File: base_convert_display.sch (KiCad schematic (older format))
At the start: 42 parts

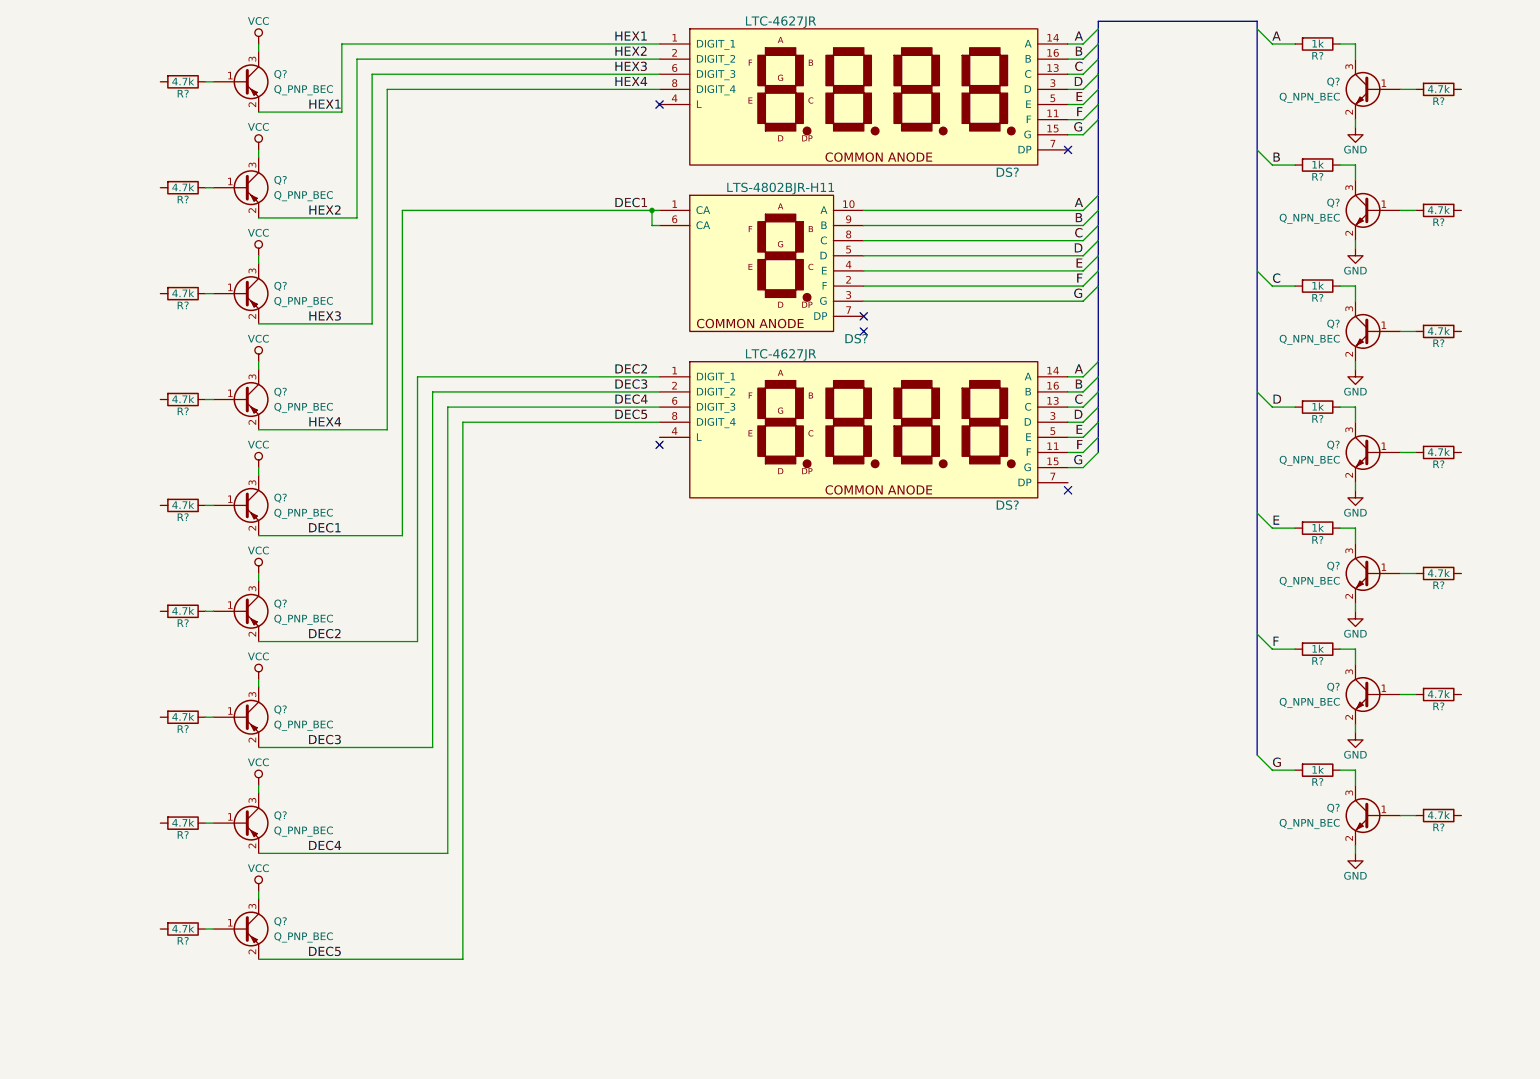
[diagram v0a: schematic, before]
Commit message: capture keypad inputs
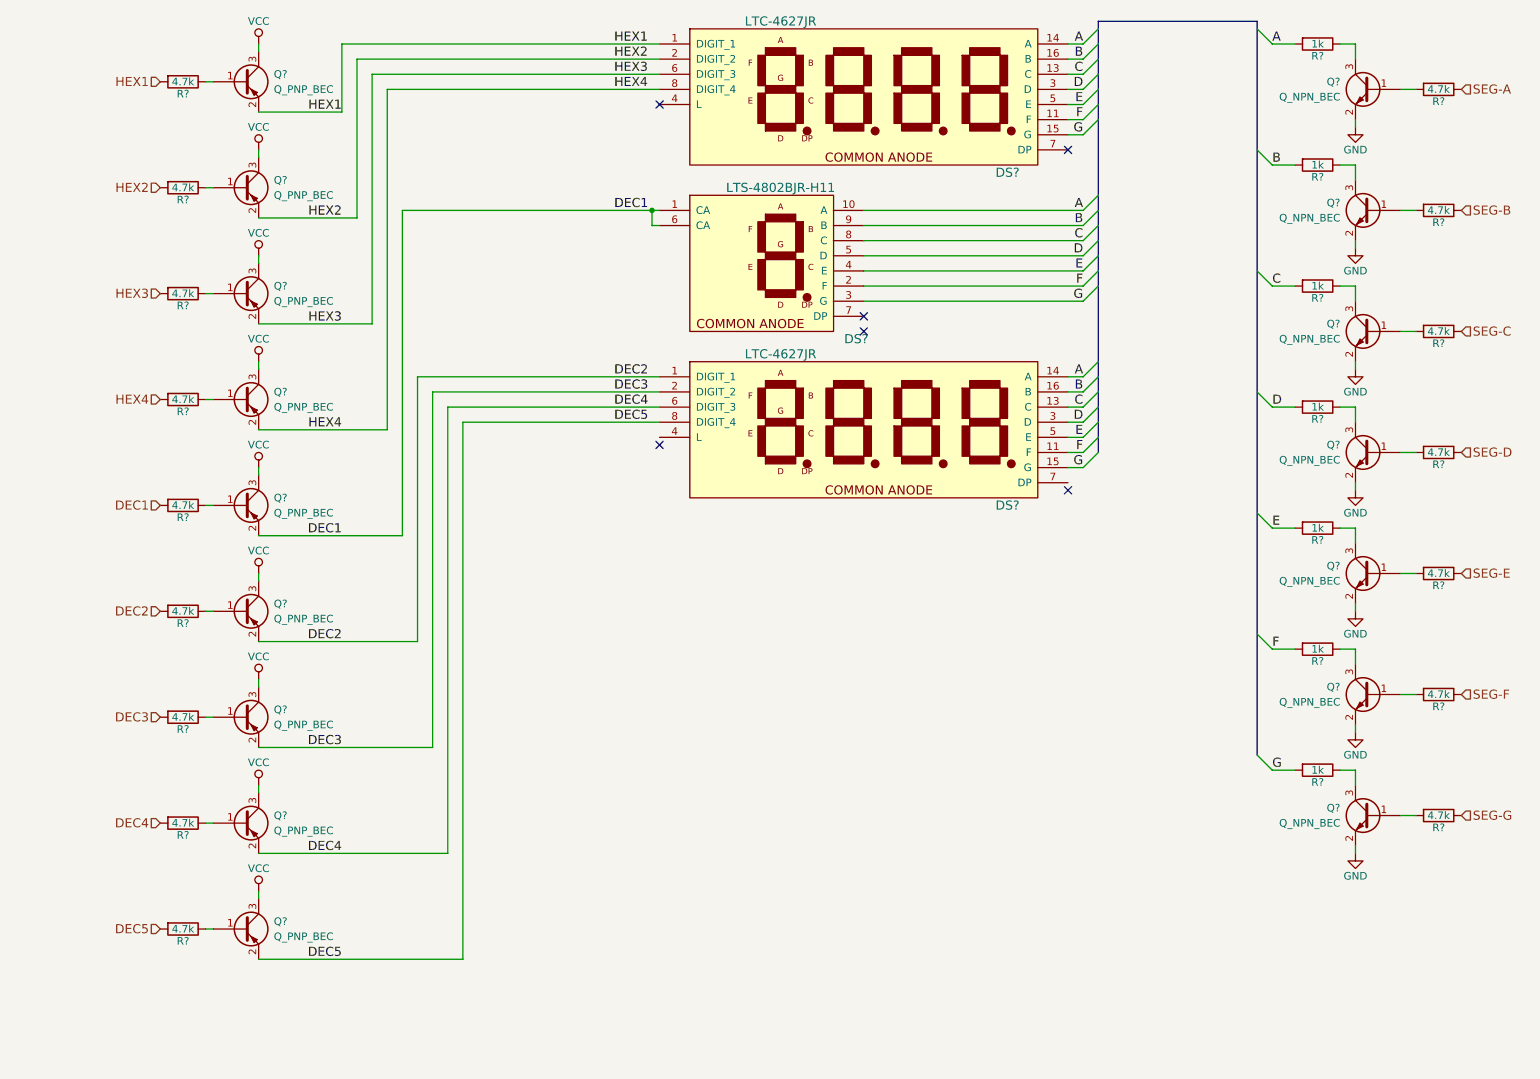
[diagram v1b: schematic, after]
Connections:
- net DEC1: now also R?.2
- net DEC2: now also R?.2
- net DEC3: now also R?.2
- net DEC4: now also R?.2
- net DEC5: now also R?.2
- net HEX1: now also R?.2
- net HEX2: now also R?.2
- net HEX3: now also R?.2
- net HEX4: now also R?.2
- net SEG-A: now reaches R?.1
- net SEG-B: now reaches R?.1
- net SEG-C: now reaches R?.1
- net SEG-D: now reaches R?.1
- net SEG-E: now reaches R?.1
- net SEG-F: now reaches R?.1
- net SEG-G: now reaches R?.1
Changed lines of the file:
@@
 $Descr A4 11693 8268
 encoding utf-8
-Sheet 3 3
-Title ""
+Sheet 2 3
+Title "Base Converter"
 Date ""
 Rev ""
-Comp ""
+Comp "Perry Leumas"
 Comment1 ""
 Comment2 ""
@@
 	2200 6750 3550 6750
 Wire Wire Line
-	3150 1800 4800 1800
-Wire Wire Line
-	4800 1800 4850 1800
+	3150 1800 4850 1800
 Wire Wire Line
 	4850 1900 4800 1900
@@
 G
 Wire Bus Line
-	7750 550  7750 700
-Wire Bus Line
-	7750 700  7750 800
-Wire Bus Line
-	7750 800  7750 900
-Wire Bus Line
-	7750 900  7750 1000
-Wire Bus Line
-	7750 1000 7750 1100
-Wire Bus Line
-	7750 1100 7750 1200
-Wire Bus Line
-	7750 1200 7750 1700
-Wire Bus Line
-	7750 1700 7750 1800
-Wire Bus Line
-	7750 1800 7750 1900
-Wire Bus Line
-	7750 1900 7750 2000
-Wire Bus Line
-	7750 2000 7750 2100
-Wire Bus Line
-	7750 2100 7750 2200
-Wire Bus Line
-	7750 2200 7750 2300
-Wire Bus Line
-	7750 2300 7750 2800
-Wire Bus Line
-	7750 2800 7750 2900
-Wire Bus Line
-	7750 2900 7750 3000
-Wire Bus Line
-	7750 3000 7750 3100
-Wire Bus Line
-	7750 3100 7750 3200
-Wire Bus Line
-	7750 3200 7750 3300
-Wire Bus Line
-	7750 3300 7750 3400
+	7750 550  7750 3400
 Entry Wire Line
 	7650 700  7750 600
@@
 Entry Wire Line
 	8800 4600 8900 4700
+Text HLabel 1550 950  0    60   Input ~ 0
+HEX1
+Text HLabel 1550 1650 0    60   Input ~ 0
+HEX2
+Text HLabel 1550 2350 0    60   Input ~ 0
+HEX3
+Text HLabel 1550 3050 0    60   Input ~ 0
+HEX4
+Text HLabel 1550 3750 0    60   Input ~ 0
+DEC1
+Text HLabel 1550 4450 0    60   Input ~ 0
+DEC2
+Text HLabel 1550 5150 0    60   Input ~ 0
+DEC3
+Text HLabel 1550 5850 0    60   Input ~ 0
+DEC4
+Text HLabel 1550 6550 0    60   Input ~ 0
+DEC5
+Text HLabel 10150 1000 2    60   Input ~ 0
+SEG-A
+Text HLabel 10150 1800 2    60   Input ~ 0
+SEG-B
+Text HLabel 10150 2600 2    60   Input ~ 0
+SEG-C
+Text HLabel 10150 3400 2    60   Input ~ 0
+SEG-D
+Text HLabel 10150 4200 2    60   Input ~ 0
+SEG-E
+Text HLabel 10150 5000 2    60   Input ~ 0
+SEG-F
+Text HLabel 10150 5800 2    60   Input ~ 0
+SEG-G
 $EndSCHEMATC

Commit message: schematic captured, footprints complete
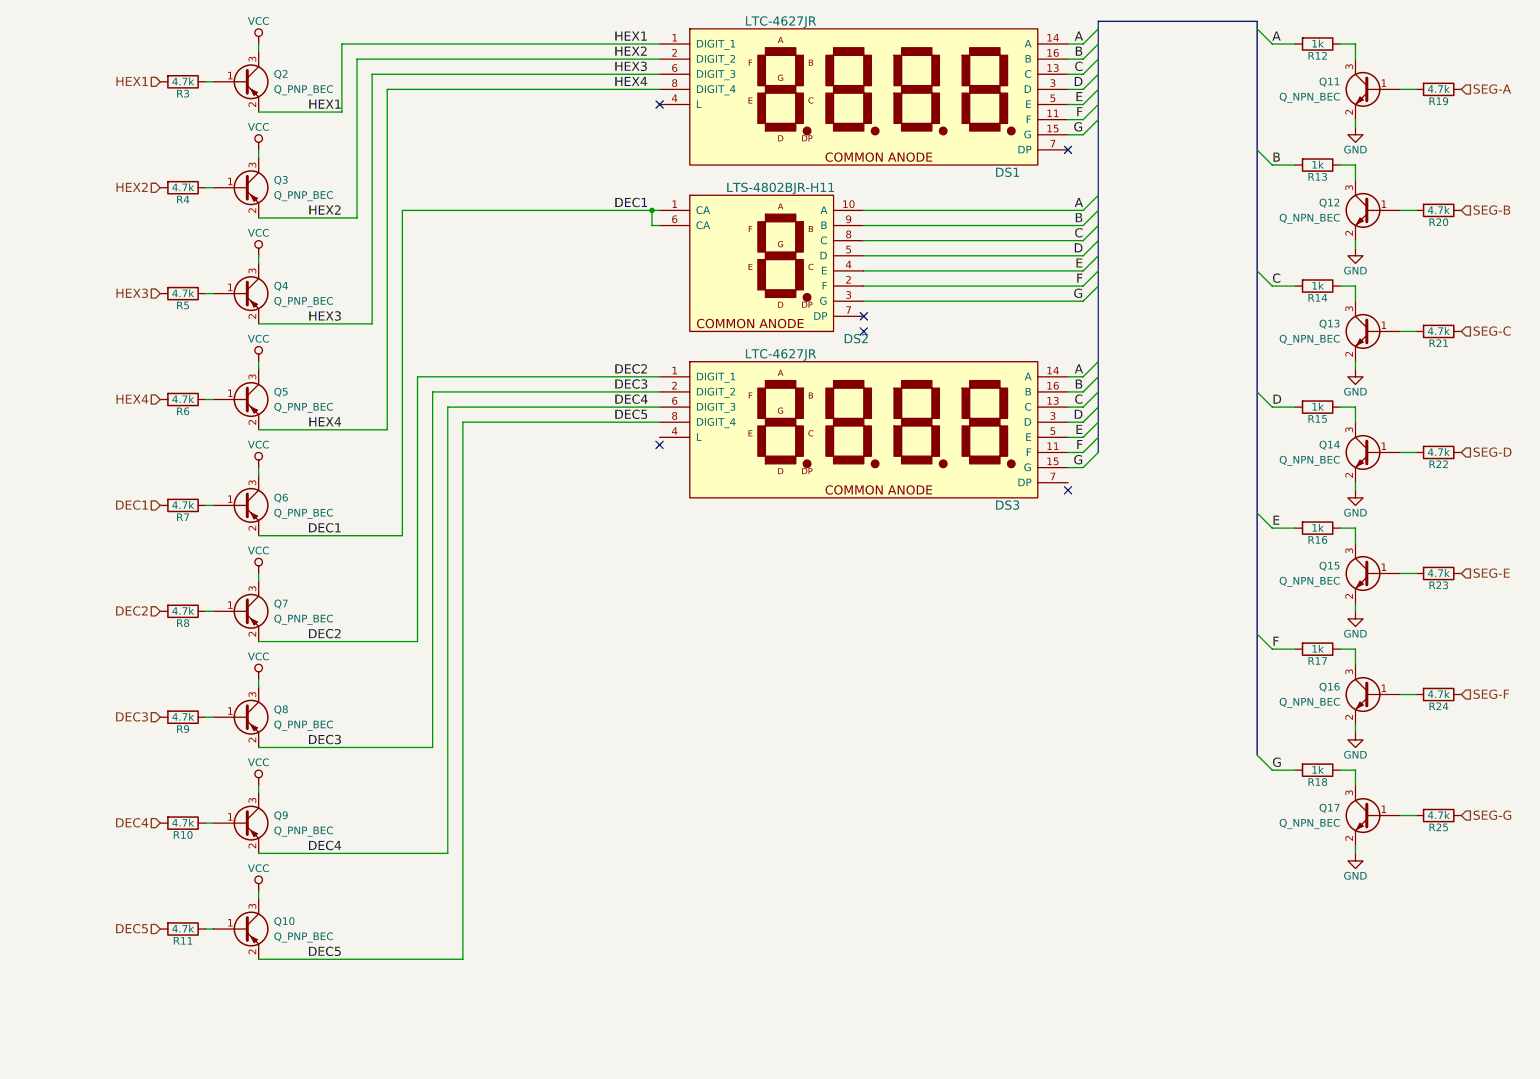
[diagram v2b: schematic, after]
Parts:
- DS1, DS3: renamed from DS?; footprint (none) -> Lite-On:LTC-4627JR; Description (none) -> NONE; Manufacture (none) -> NONE; Mfg Part Number (none) -> NONE; Package (none) -> NONE
- DS2: renamed from DS?; footprint (none) -> Lite-On:LTS-4802BJR-H1; Description (none) -> NONE; Manufacture (none) -> NONE; Mfg Part Number (none) -> NONE; Package (none) -> NONE
- Q10, Q11, Q12, Q13, Q14, Q15, Q16, Q17, Q2, Q3, Q4, Q5, Q6, Q7, Q8, Q9: renamed from Q?; footprint (none) -> TO_SOT_Packages_SMD:SOT-23
- R10, R11, R19, R20, R21, R22, R23, R24, R25, R3, R4, R5, R6, R7, R8, R9: renamed from R?; footprint (none) -> Resistors_SMD:R_0805
- R12, R13, R14, R15, R16, R17, R18: renamed from R?; footprint (none) -> Resistors_SMD:R_0603

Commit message: update 7-segment display part number
Due to mismatch of display face using a mix of 4 digit and 1 digit displays does not look good. Swtiching all displays to be made up of 2 digit 7-segment display. Decimal display will have extra unused digit.
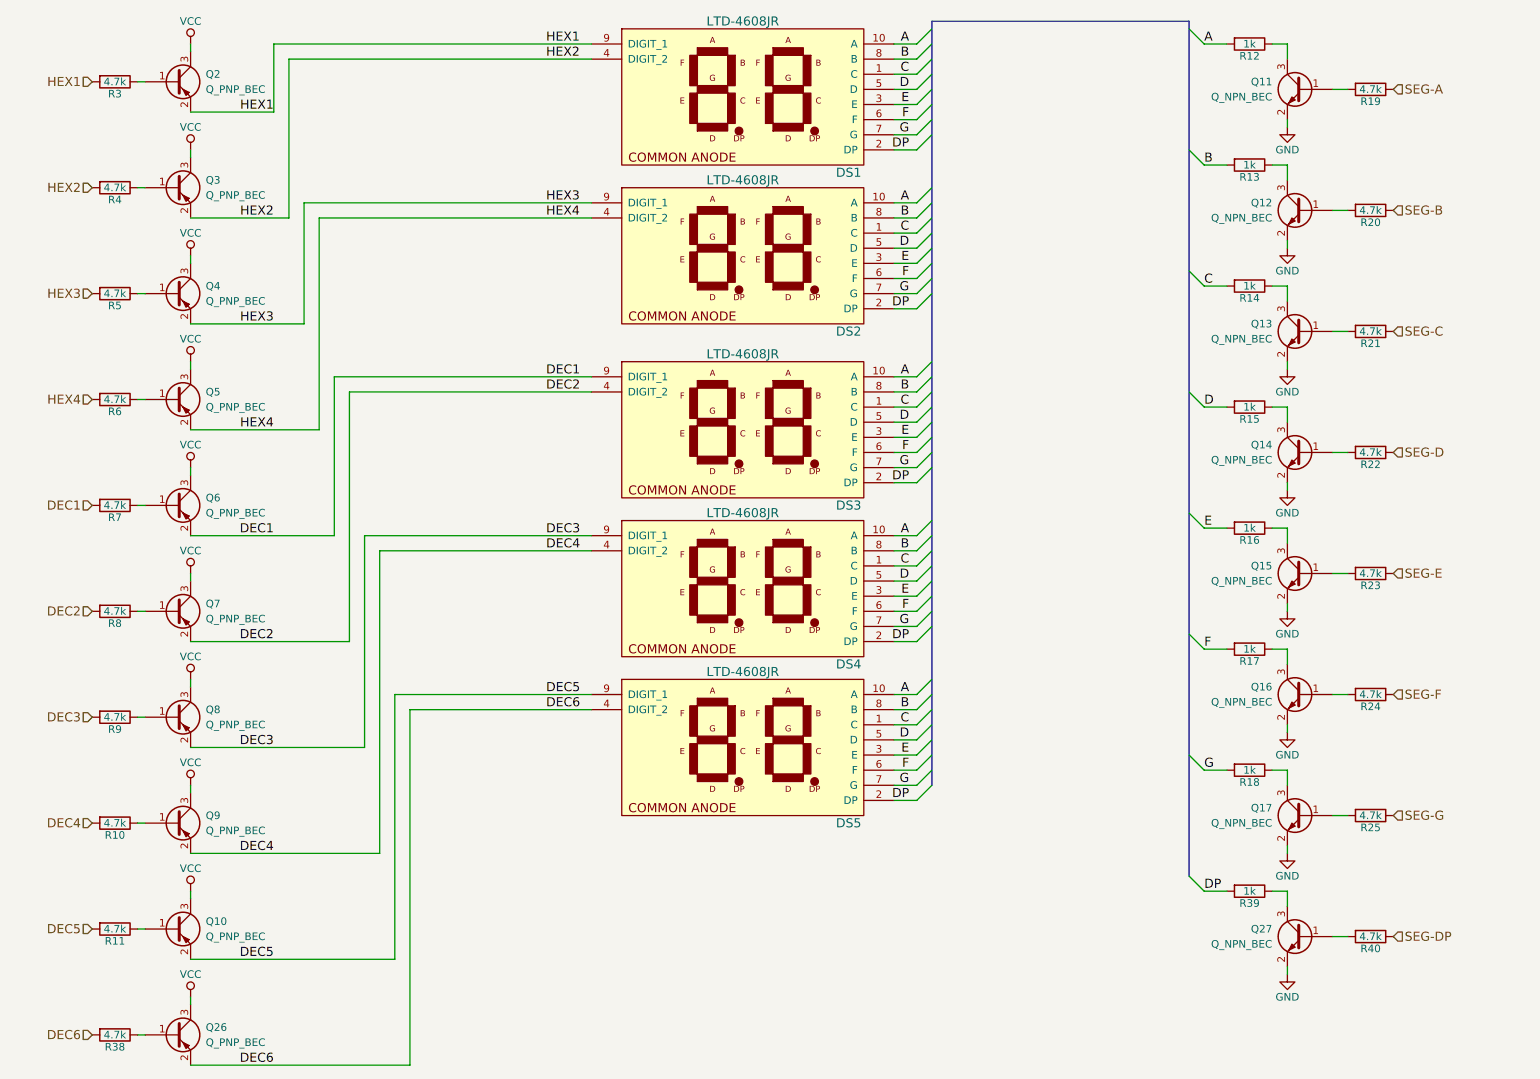
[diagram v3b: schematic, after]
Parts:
- removed DS1, DS3: LTC-4627JR, Lite-On:LTC-4627JR, symbol LTC-4627JR
- removed DS2: LTS-4802BJR-H11, Lite-On:LTS-4802BJR-H1, symbol LTS-4802BJR-H11
- added DS1, DS2, DS3, DS4, DS5: LTD-4608JR, Lite-On:Display_Lite-On_LTD-4608JR, symbol LTD-4608JR
- added Q26: Q_PNP_BEC, TO_SOT_Packages_SMD:SOT-23, symbol Q_PNP_BEC
- added Q27: Q_NPN_BEC, TO_SOT_Packages_SMD:SOT-23, symbol Q_NPN_BEC
- added R38, R40: 4.7k, Resistors_SMD:R_0805, symbol R
- added R39: 1k, Resistors_SMD:R_0603, symbol R
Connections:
- net A: now also DS1.10 (A), DS2.10 (A), DS3.10 (A), DS4.10 (A), DS5.10 (A)
- net B: now also DS1.8 (B), DS2.8 (B), DS3.8 (B), DS4.8 (B), DS5.8 (B)
- net C: now also DS1.1 (C), DS2.1 (C), DS3.1 (C), DS4.1 (C), DS5.1 (C)
- net D: now also DS1.5 (D), DS2.5 (D), DS3.5 (D), DS4.5 (D), DS5.5 (D)
- net DEC1: now also DS3.9 (DIGIT_1)
- net DEC2: now also DS3.4 (DIGIT_2)
- net DEC3: now also DS4.9 (DIGIT_1)
- net DEC4: now also DS4.4 (DIGIT_2)
- net DEC5: now also DS5.9 (DIGIT_1)
- net E: now also DS1.3 (E), DS2.3 (E), DS3.3 (E), DS4.3 (E), DS5.3 (E)
- net F: now also DS1.6 (F), DS2.6 (F), DS3.6 (F), DS4.6 (F), DS5.6 (F)
- net G: now also DS1.7 (G), DS2.7 (G), DS3.7 (G), DS4.7 (G), DS5.7 (G)
- net GND: now also Q27.2 (E)
- net HEX1: now also DS1.9 (DIGIT_1)
- net HEX2: now also DS1.4 (DIGIT_2)
- net HEX3: now also DS2.9 (DIGIT_1)
- net HEX4: now also DS2.4 (DIGIT_2)
- net VCC: now also Q26.3 (C)
- new net: Q26.1 (B), R38.1
- new net: Q27.1 (B), R40.2
- new net: Q27.3 (C), R39.1
- new net DEC6: DS5.4 (DIGIT_2), Q26.2 (E), R38.2
- new net DP: DS1.2 (DP), DS2.2 (DP), DS3.2 (DP), DS4.2 (DP), DS5.2 (DP), R39.2
- new net SEG-DP: R40.1
- no-connect marks 6 -> 0
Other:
- moved on the sheet: Q10, Q11, Q12, Q13, Q14, Q15, Q16, Q17, Q2, Q3, Q4, Q5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

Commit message: updated shema fields. Raplced tack switch with 4 pin footprint
Using 4 pin tack switch to ease pcb layout connecitions. Also updated component fields in schema
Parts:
- DS1:  H 6100 650 50 0001 C CNN  (none) -> 10-DIP (0.400; Manufacture (none) -> Lite-On Inc.; Mfg Part Number (none) -> LTD-4608JR
- DS2:  H 6100 1700 50 0001 C CNN  (none) -> 10-DIP (0.400; Manufacture (none) -> Lite-On Inc.; Mfg Part Number (none) -> LTD-4608JR
- DS3:  H 6100 2850 50 0001 C CNN  (none) -> 10-DIP (0.400; Manufacture (none) -> Lite-On Inc.; Mfg Part Number (none) -> LTD-4608JR
- DS4:  H 6100 3900 50 0001 C CNN  (none) -> 10-DIP (0.400; Manufacture (none) -> Lite-On Inc.; Mfg Part Number (none) -> LTD-4608JR
- DS5:  H 6100 4950 50 0001 C CNN  (none) -> 10-DIP (0.400; Manufacture (none) -> Lite-On Inc.; Mfg Part Number (none) -> LTD-4608JR
- Q10, Q26, Q3: Description (none) -> TRANS PNP 40V 0.2A SOT23; Manufacture (none) -> Nexperia USA Inc.; Mfg Part Number (none) -> PMBT3906,235; Package (none) -> SOT-23
- Q11, Q12, Q13, Q14, Q15, Q16, Q17, Q27: Description (none) -> TRANSISTOR, NPN, 40V, 0.2A, 100A; Manufacture (none) -> Taiwan Semiconductor Corporation; Mfg Part Number (none) -> MMBT3904L RFG; Package (none) -> SOT-23
- Q2, Q5: Description (none) -> TRANS PNP 40V 0.2A SOT25; Manufacture (none) -> Nexperia USA Inc.; Mfg Part Number (none) -> PMBT3906,237; Package (none) -> SOT-23
- Q4: Description (none) -> TRANS PNP 40V 0.2A SOT24; Manufacture (none) -> Nexperia USA Inc.; Mfg Part Number (none) -> PMBT3906,236; Package (none) -> SOT-23
- Q6: Description (none) -> TRANS PNP 40V 0.2A SOT26; Manufacture (none) -> Nexperia USA Inc.; Mfg Part Number (none) -> PMBT3906,238; Package (none) -> SOT-23
- Q7: Description (none) -> TRANS PNP 40V 0.2A SOT27; Manufacture (none) -> Nexperia USA Inc.; Mfg Part Number (none) -> PMBT3906,239; Package (none) -> SOT-23
- Q8: Description (none) -> TRANS PNP 40V 0.2A SOT28; Manufacture (none) -> Nexperia USA Inc.; Mfg Part Number (none) -> PMBT3906,240; Package (none) -> SOT-23
- Q9: Description (none) -> TRANS PNP 40V 0.2A SOT29; Manufacture (none) -> Nexperia USA Inc.; Mfg Part Number (none) -> PMBT3906,241; Package (none) -> SOT-23
- R10, R11, R12, R13, R14, R15, R16, R17, R18, R19, R20, R21, R22, R23, R24, R25, R3, R38, R39, R4, R40, R5, R6, R7, R8, R9: Description NONE -> (none); Manufacture NONE -> (none); Mfg Part Number NONE -> (none); Package NONE -> (none)
